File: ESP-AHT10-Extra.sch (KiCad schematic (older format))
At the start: 19 parts, among them J1 USB, SW1 RESET, SW2 PROG, U1 CH330N, U2 HT7233, U3 ESP-12, U4 AHT10

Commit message: 3mm shorter
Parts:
- SW1, SW2: footprint CPB:SW_PUSH_4.5mm -> CPB:Tact Switch 6mmx3.5mm C318817
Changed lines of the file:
@@
 F 0 "SW2" V 4104 6548 50  0000 L CNN
 F 1 "PROG" V 4195 6548 50  0000 L CNN
-F 2 "CPB:SW_PUSH_4.5mm" H 4150 6600 50  0001 C CNN
+F 2 "CPB:Tact Switch 6mmx3.5mm C318817" H 4150 6600 50  0001 C CNN
 F 3 "" H 4150 6600 50  0001 C CNN
 	1    4150 6400
@@
 F 0 "SW1" V 1504 6548 50  0000 L CNN
 F 1 "RESET" V 1595 6548 50  0000 L CNN
-F 2 "CPB:SW_PUSH_4.5mm" H 1550 6600 50  0001 C CNN
+F 2 "CPB:Tact Switch 6mmx3.5mm C318817" H 1550 6600 50  0001 C CNN
 F 3 "" H 1550 6600 50  0001 C CNN
 	1    1550 6400

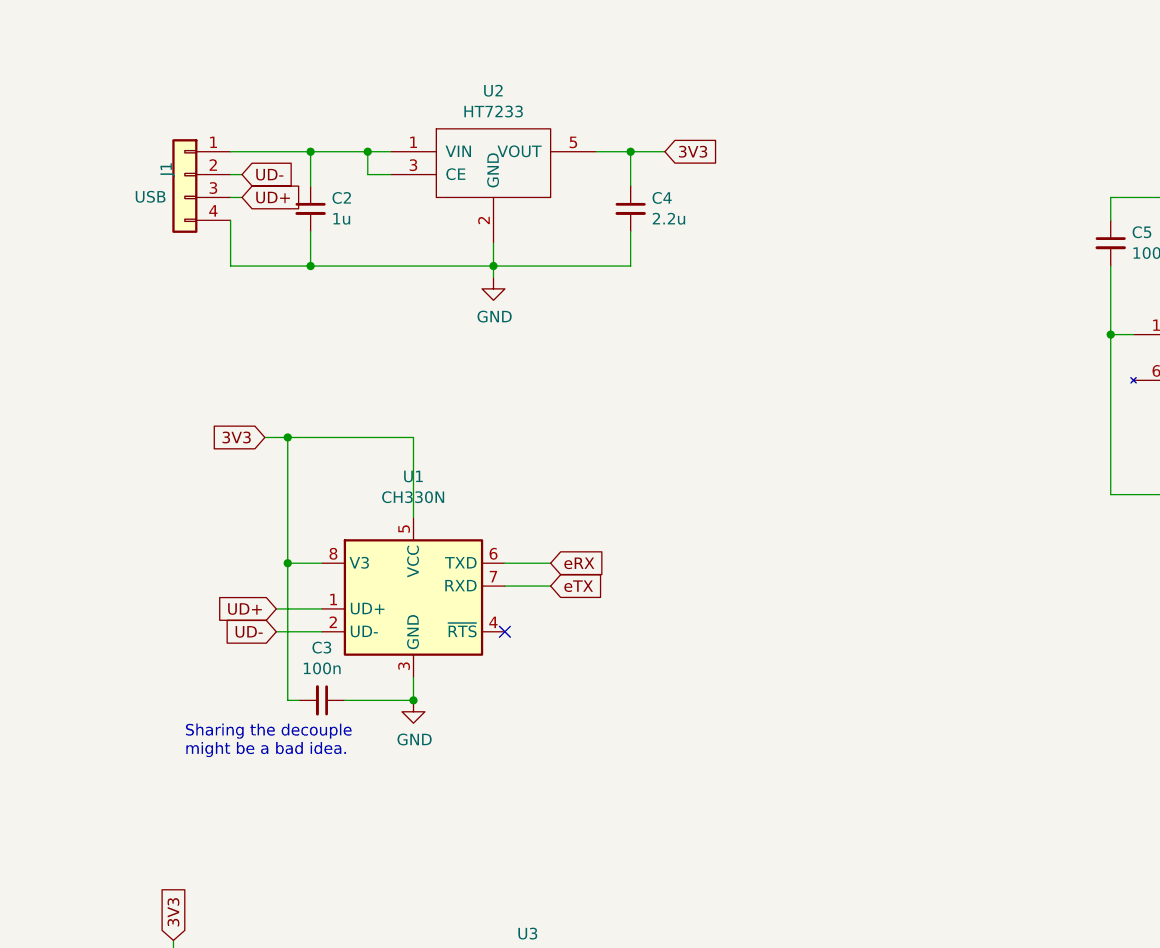
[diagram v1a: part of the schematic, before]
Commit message: add USB ESD protection
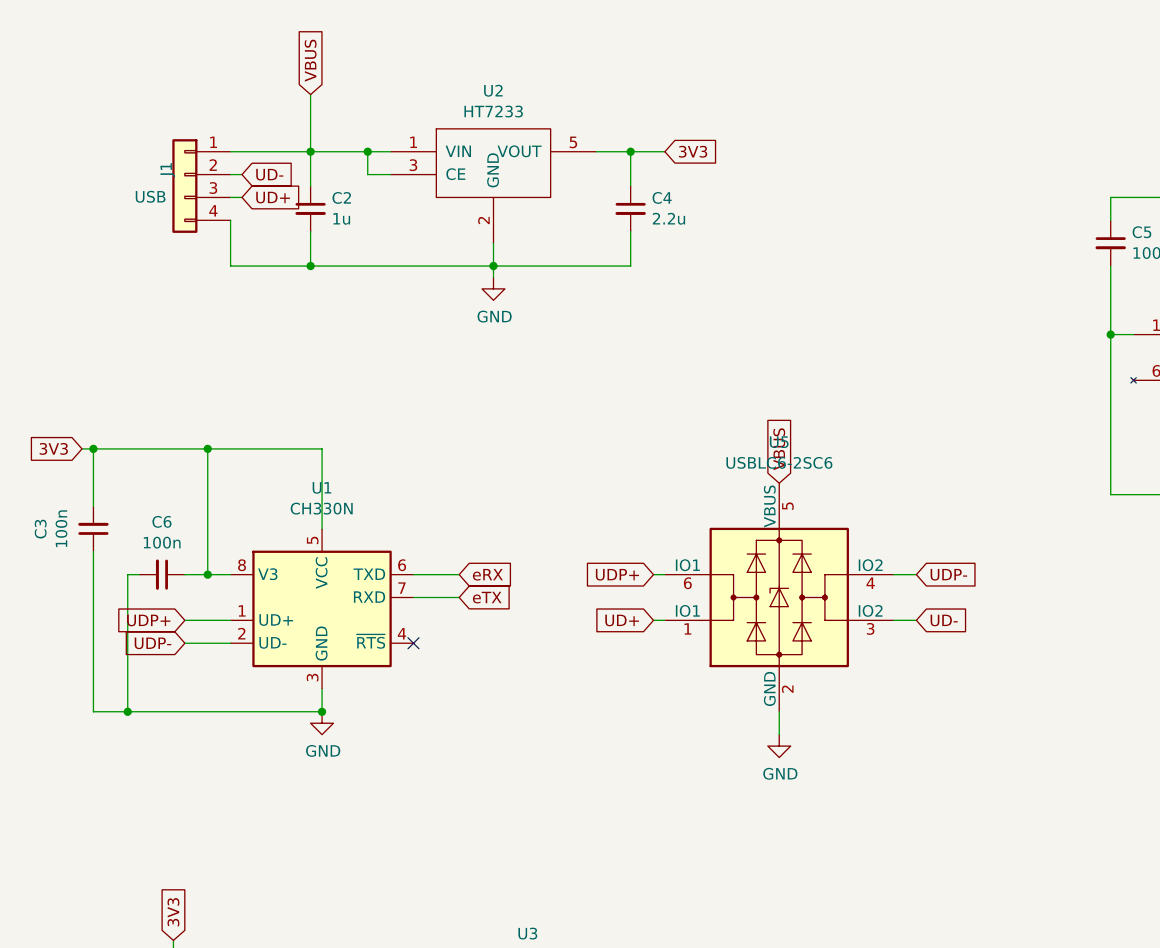
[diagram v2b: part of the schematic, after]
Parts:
- added C6: 100n, Capacitors_SMD:C_0805, symbol Device:C_Small
- added U5: USBLC6-2SC6, Package_TO_SOT_SMD:SOT-23-6, symbol Power_Protection:USBLC6-2SC6
- U4: footprint CPB:AHT10 -> CPB:AHT10-HandSolder
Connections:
- net 3V3: now also C6.1
- net GND: now also C6.2, U5.2 (GND)
- net UD+: now also U5.1 (IO1); no longer U1.1 (UD+)
- net UD-: now also U5.3 (IO2); no longer U1.2 (UD-)
- net VBUS: now reaches C2.1, J1.1 (Pin_1), U2.1 (VIN), U2.3 (CE)
- net VBUS: now also U5.5 (VBUS)
- new net UDP+: U1.1 (UD+), U5.6 (IO1)
- new net UDP-: U1.2 (UD-), U5.4 (IO2)
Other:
- note removed: "Sharing the decouple\nmight be a bad idea."
- moved on the sheet: C3, U1
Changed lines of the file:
@@
 F 0 "U4" H 5650 1750 50  0000 C CNN
 F 1 "AHT10" H 6300 1750 50  0000 C CNN
-F 2 "CPB:AHT10" H 6000 2200 50  0001 C CNN
+F 2 "CPB:AHT10-HandSolder" H 6000 2200 50  0001 C CNN
 F 3 "" H 6000 2200 50  0001 C CNN
 	1    6000 2200
@@
 L Interface_USB:CH330N U1
 U 1 1 5DC02823
-P 2250 3200
-F 0 "U1" H 2250 3678 50  0000 C CNN
-F 1 "CH330N" H 2250 3587 50  0000 C CNN
-F 2 "Package_SO:SOIC-8_3.9x4.9mm_P1.27mm" H 2100 3950 50  0001 C CNN
-F 3 "http://www.wch.cn/downloads/file/240.html" H 2150 3400 50  0001 C CNN
-	1    2250 3200
+P 1850 3250
+F 0 "U1" H 1850 3728 50  0000 C CNN
+F 1 "CH330N" H 1850 3637 50  0000 C CNN
+F 2 "Package_SO:SOIC-8_3.9x4.9mm_P1.27mm" H 1700 4000 50  0001 C CNN
+F 3 "http://www.wch.cn/downloads/file/240.html" H 1750 3450 50  0001 C CNN
+	1    1850 3250
 	1    0    0    -1
 $EndComp
@@
 Wire Wire Line
 	1450 1500 1500 1500
-Text GLabel 1650 3400 0    50   Input ~ 0
+Text GLabel 4450 3350 2    50   Input ~ 0
 UD-
-Text GLabel 1650 3300 0    50   Input ~ 0
+Text GLabel 3300 3350 0    50   Input ~ 0
 UD+
 Wire Wire Line
-	1650 3300 1850 3300
-Wire Wire Line
-	1650 3400 1850 3400
-NoConn ~ 2650 3400
+	1250 3350 1450 3350
+Wire Wire Line
+	1250 3450 1450 3450
+NoConn ~ 2250 3450
 $Comp
 L power:GND #PWR01
 U 1 1 5DC098ED
-P 2250 3700
-F 0 "#PWR01" H 2250 3450 50  0001 C CNN
-F 1 "GND" H 2255 3527 50  0000 C CNN
-F 2 "" H 2250 3700 50  0001 C CNN
-F 3 "" H 2250 3700 50  0001 C CNN
-	1    2250 3700
-	1    0    0    -1
-$EndComp
-Text GLabel 1600 2550 0    50   Input ~ 0
+P 1850 3750
+F 0 "#PWR01" H 1850 3500 50  0001 C CNN
+F 1 "GND" H 1855 3577 50  0000 C CNN
+F 2 "" H 1850 3750 50  0001 C CNN
+F 3 "" H 1850 3750 50  0001 C CNN
+	1    1850 3750
+	1    0    0    -1
+$EndComp
+Text GLabel 800  2600 0    50   Input ~ 0
 3V3
 Wire Wire Line
-	1600 2550 1700 2550
-Wire Wire Line
-	2250 2550 2250 2900
-Wire Wire Line
-	1700 2550 1700 3100
-Wire Wire Line
-	1700 3100 1850 3100
-Connection ~ 1700 2550
-Wire Wire Line
-	1700 2550 2250 2550
+	1850 2600 1850 2950
 $Comp
 L Device:C_Small C3
 U 1 1 5DC0C395
-P 1850 3700
-F 0 "C3" V 1621 3700 50  0000 C CNN
-F 1 "100n" V 1712 3700 50  0000 C CNN
-F 2 "Capacitors_SMD:C_0805" H 1850 3700 50  0001 C CNN
-F 3 "~" H 1850 3700 50  0001 C CNN
-	1    1850 3700
-	0    1    1    0
-$EndComp
-Wire Wire Line
-	1700 3100 1700 3700
-Wire Wire Line
-	1700 3700 1750 3700
-Connection ~ 1700 3100
-Wire Wire Line
-	1950 3700 2250 3700
-Wire Wire Line
-	2250 3600 2250 3700
-Connection ~ 2250 3700
-Text GLabel 2850 3200 2    50   Input ~ 0
+P 850 2950
+F 0 "C3" V 621 2950 50  0000 C CNN
+F 1 "100n" V 712 2950 50  0000 C CNN
+F 2 "Capacitors_SMD:C_0805" H 850 2950 50  0001 C CNN
+F 3 "~" H 850 2950 50  0001 C CNN
+	1    850  2950
+	1    0    0    1
+$EndComp
+Wire Wire Line
+	1850 3650 1850 3750
+Connection ~ 1850 3750
+Text GLabel 2450 3250 2    50   Input ~ 0
 eTX
-Text GLabel 2850 3100 2    50   Input ~ 0
+Text GLabel 2450 3150 2    50   Input ~ 0
 eRX
 Wire Wire Line
-	2650 3100 2850 3100
-Wire Wire Line
-	2650 3200 2850 3200
+	2250 3150 2450 3150
+Wire Wire Line
+	2250 3250 2450 3250
 $Comp
 L Switch:SW_Push SW2
@@
 Wire Wire Line
 	1550 6700 2750 6700
-Text Notes 1250 3950 0    50   ~ 0
-Sharing the decouple\nmight be a bad idea.
+$Comp
+L Device:C_Small C6
+U 1 1 5DC2141A
+P 1150 3150
+F 0 "C6" V 921 3150 50  0000 C CNN
+F 1 "100n" V 1012 3150 50  0000 C CNN
+F 2 "Capacitors_SMD:C_0805" H 1150 3150 50  0001 C CNN
+F 3 "~" H 1150 3150 50  0001 C CNN
+	1    1150 3150
+	0    1    1    0
+$EndComp
+Wire Wire Line
+	800  2600 850  2600
+Wire Wire Line
+	850  2850 850  2600
+Connection ~ 850  2600
+Wire Wire Line
+	850  3050 850  3750
+Wire Wire Line
+	850  3750 1000 3750
+Wire Wire Line
+	1050 3150 1000 3150
+Wire Wire Line
+	1000 3150 1000 3750
+Wire Wire Line
+	1000 3750 1850 3750
+$Comp
+L Power_Protection:USBLC6-2SC6 U5
+U 1 1 5DC39FB1
+P 3850 3250
+F 0 "U5" H 3850 3928 50  0000 C CNN
+F 1 "USBLC6-2SC6" H 3850 3837 50  0000 C CNN
+F 2 "Package_TO_SOT_SMD:SOT-23-6" H 3100 3650 50  0001 C CNN
+F 3 "http://www2.st.com/resource/en/datasheet/CD00050750.pdf" H 4050 3600 50  0001 C CNN
+	1    3850 3250
+	1    0    0    -1
+$EndComp
+Text GLabel 1250 3350 0    50   Input ~ 0
+UDP+
+Text GLabel 1250 3450 0    50   Input ~ 0
+UDP-
+Connection ~ 1000 3750
+Wire Wire Line
+	1250 3150 1350 3150
+$Comp
+L power:GND #PWR05
+U 1 1 5DC4A8A6
+P 3850 3850
+F 0 "#PWR05" H 3850 3600 50  0001 C CNN
+F 1 "GND" H 3855 3677 50  0000 C CNN
+F 2 "" H 3850 3850 50  0001 C CNN
+F 3 "" H 3850 3850 50  0001 C CNN
+	1    3850 3850
+	1    0    0    -1
+$EndComp
+Wire Wire Line
+	1800 1050 1800 1300
+Text GLabel 1800 1050 1    50   Input ~ 0
+VBUS
+Text GLabel 3850 2750 1    50   Input ~ 0
+VBUS
+Text GLabel 3300 3150 0    50   Input ~ 0
+UDP+
+Text GLabel 4450 3150 2    50   Input ~ 0
+UDP-
+Wire Wire Line
+	3300 3150 3350 3150
+Wire Wire Line
+	3300 3350 3350 3350
+Wire Wire Line
+	4350 3150 4450 3150
+Wire Wire Line
+	4350 3350 4450 3350
+Wire Wire Line
+	3850 3750 3850 3850
+Wire Wire Line
+	850  2600 1350 2600
+Wire Wire Line
+	1350 2600 1350 3150
+Connection ~ 1350 2600
+Wire Wire Line
+	1350 2600 1850 2600
+Connection ~ 1350 3150
+Wire Wire Line
+	1350 3150 1450 3150
 $EndSCHEMATC

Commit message: add a fuse. Don't need to fry another sensor...
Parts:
- added F1: 500mA, Fuse:Fuse_0805_2012Metric, symbol Device:Fuse_Small
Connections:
- wire segments 97 -> 100
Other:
- moved on the sheet: J1
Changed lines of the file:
@@
 L Connector_Generic:Conn_01x04 J1
 U 1 1 5DBDB3F6
-P 1250 1400
-F 0 "J1" V 1330 1392 50  0000 L CNN
-F 1 "USB" H 1330 1301 50  0000 L CNN
-F 2 "CPB:usb-PCB" H 1250 1400 50  0001 C CNN
-F 3 "~" H 1250 1400 50  0001 C CNN
-	1    1250 1400
+P 900 1400
+F 0 "J1" V 980 1392 50  0000 L CNN
+F 1 "USB" H 980 1301 50  0000 L CNN
+F 2 "CPB:usb-PCB" H 900 1400 50  0001 C CNN
+F 3 "~" H 900 1400 50  0001 C CNN
+	1    900  1400
 	-1   0    0    -1
 $EndComp
@@
 Wire Wire Line
 	1800 1300 1800 1450
-Connection ~ 1800 1300
 Wire Wire Line
 	1800 1300 2050 1300
@@
 	1450 1800 1800 1800
 Connection ~ 1800 1800
-Wire Wire Line
-	1450 1300 1800 1300
 Text GLabel 7000 2300 2    50   Input ~ 0
 SCL
@@
 Text GLabel 1500 1500 2    50   Input ~ 0
 UD+
-Wire Wire Line
-	1450 1400 1500 1400
-Wire Wire Line
-	1450 1500 1500 1500
 Text GLabel 4450 3350 2    50   Input ~ 0
 UD-
@@
 	1    0    0    -1
 $EndComp
-Wire Wire Line
-	1800 1050 1800 1300
-Text GLabel 1800 1050 1    50   Input ~ 0
+Text GLabel 2100 1050 2    50   Output ~ 0
 VBUS
 Text GLabel 3850 2750 1    50   Input ~ 0
@@
 Wire Wire Line
 	1350 3150 1450 3150
+$Comp
+L Device:Fuse_Small F1
+U 1 1 5DC64535
+P 1400 1300
+F 0 "F1" H 1400 1485 50  0000 C CNN
+F 1 "500mA" H 1400 1394 50  0000 C CNN
+F 2 "Fuse:Fuse_0805_2012Metric" H 1400 1300 50  0001 C CNN
+F 3 "~" H 1400 1300 50  0001 C CNN
+	1    1400 1300
+	1    0    0    -1
+$EndComp
+Wire Wire Line
+	1100 1300 1300 1300
+Wire Wire Line
+	1100 1400 1500 1400
+Wire Wire Line
+	1100 1500 1500 1500
+Wire Wire Line
+	1100 1600 1450 1600
+Wire Wire Line
+	1500 1300 1800 1300
+Connection ~ 1800 1300
+Wire Wire Line
+	2050 1050 2050 1300
+Wire Wire Line
+	2050 1050 2100 1050
 $EndSCHEMATC

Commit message: more tweaking
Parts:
- removed F1: 500mA, Fuse:Fuse_0805_2012Metric, symbol Device:Fuse_Small
- added C7: 100n, Capacitors_SMD:C_0805, symbol Device:C_Small
- added F1: 200mA, Fuse:Fuse_0805_2012Metric, symbol Device:Polyfuse_Small
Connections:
- net labels added: 5V
- wire segments 100 -> 101
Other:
- note added: "NOTE: maybe overkill; I can't\nfind an example of a board\nwith WCH chips and ESD\nprotection.\nTermination resistors (22R?)\nmight also not be a bad idea."
- moved on the sheet: C2, C3, C4, C5, C6, J1, R6, R7, U1, U2, U4, U5

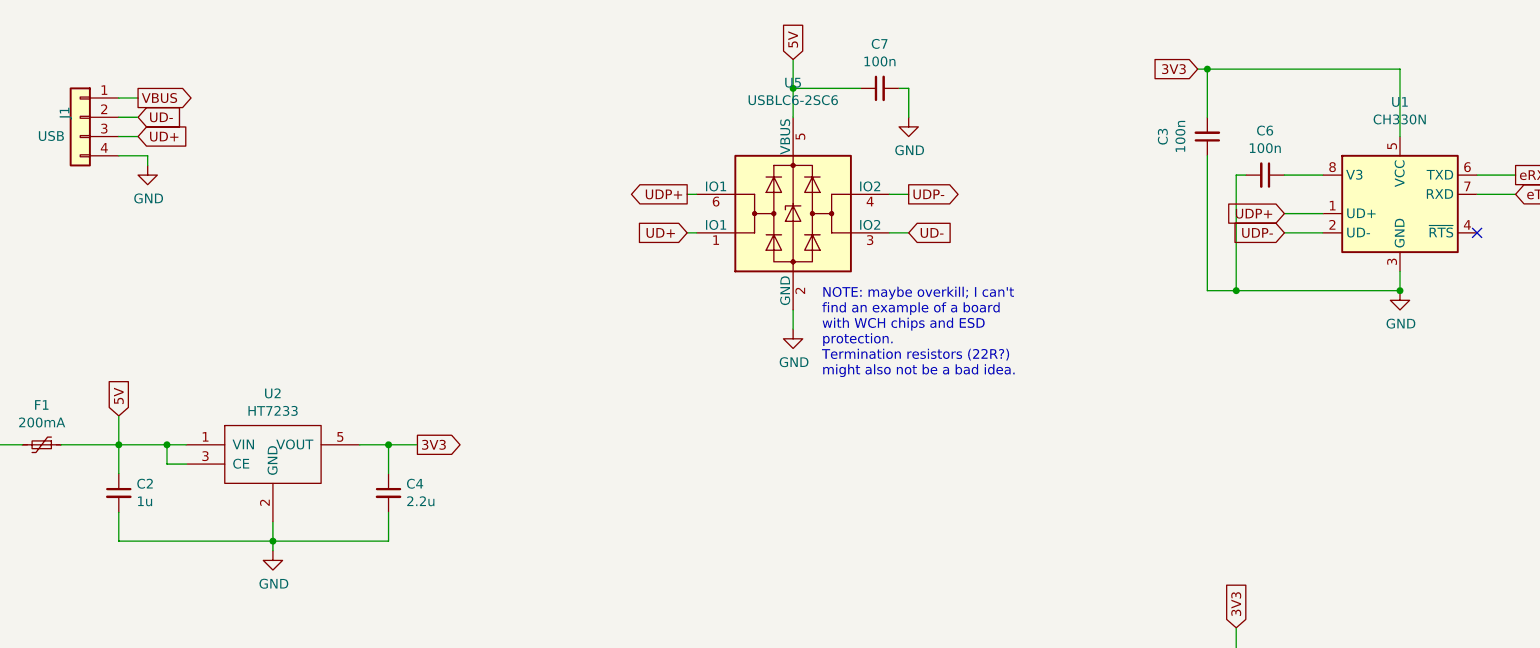
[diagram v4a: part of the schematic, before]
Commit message: fix V3 connections to CH330N, bump the bulk caps to 10uF, rev number
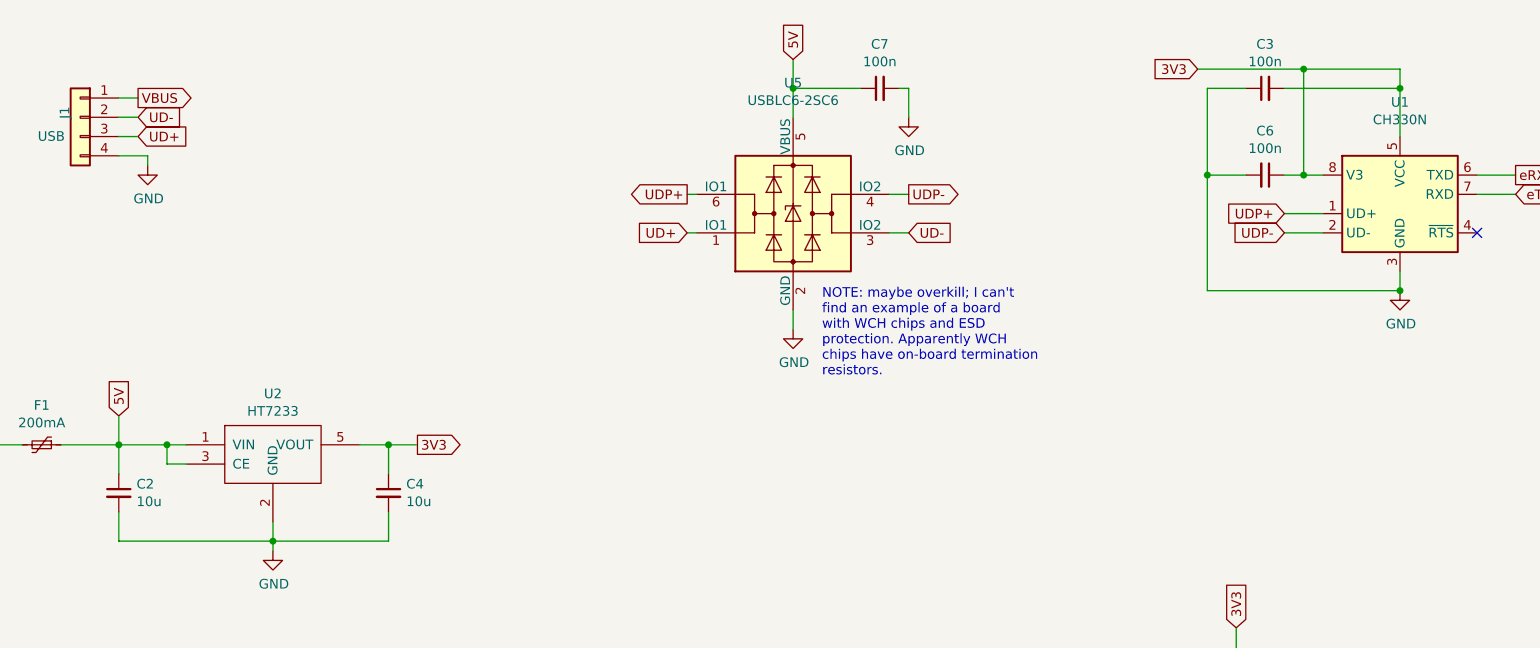
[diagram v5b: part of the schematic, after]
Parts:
- C2: value 1u -> 10u
- C4: value 2.2u -> 10u
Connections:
- net 3V3: now also C6.1, U1.8 (V3)
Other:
- note added: "NOTE: maybe overkill; I can't\nfind an example of a board\nwith WCH chips and ESD\nprotection. Apparently WCH\nchips have on-board termination\nresistors."
- note removed: "NOTE: maybe overkill; I can't\nfind an example of a board\nwith WCH chips and ESD\nprotection.\nTermination resistors (22R?)\nmight also not be a bad idea."
- moved on the sheet: C3
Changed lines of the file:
@@
 P 1950 3300
 F 0 "C2" H 2042 3346 50  0000 L CNN
-F 1 "1u" H 2042 3255 50  0000 L CNN
+F 1 "10u" H 2042 3255 50  0000 L CNN
 F 2 "Capacitors_SMD:C_0805" H 1950 3300 50  0001 C CNN
 F 3 "~" H 1950 3300 50  0001 C CNN
@@
 P 3350 3300
 F 0 "C4" H 3442 3346 50  0000 L CNN
-F 1 "2.2u" H 3442 3255 50  0000 L CNN
+F 1 "10u" H 3442 3255 50  0000 L CNN
 F 2 "Capacitors_SMD:C_0805" H 3350 3300 50  0001 C CNN
 F 3 "~" H 3350 3300 50  0001 C CNN
@@
 3V3
 Wire Wire Line
-	8600 1100 8600 1450
+	8600 1100 8600 1200
 $Comp
 L Device:C_Small C3
 U 1 1 5DC0C395
-P 7600 1450
-F 0 "C3" V 7371 1450 50  0000 C CNN
-F 1 "100n" V 7462 1450 50  0000 C CNN
-F 2 "Capacitors_SMD:C_0805" H 7600 1450 50  0001 C CNN
-F 3 "~" H 7600 1450 50  0001 C CNN
-	1    7600 1450
-	1    0    0    1
+P 7900 1200
+F 0 "C3" V 7671 1200 50  0000 C CNN
+F 1 "100n" V 7762 1200 50  0000 C CNN
+F 2 "Capacitors_SMD:C_0805" H 7900 1200 50  0001 C CNN
+F 3 "~" H 7900 1200 50  0001 C CNN
+	1    7900 1200
+	0    -1   1    0
 $EndComp
 Wire Wire Line
@@
 	0    1    1    0
 $EndComp
-Wire Wire Line
-	7550 1100 7600 1100
-Wire Wire Line
-	7600 1350 7600 1100
-Connection ~ 7600 1100
-Wire Wire Line
-	7600 1550 7600 2250
-Wire Wire Line
-	7600 2250 7750 2250
-Wire Wire Line
-	7800 1650 7750 1650
-Wire Wire Line
-	7750 1650 7750 2250
-Wire Wire Line
-	7750 2250 8600 2250
 $Comp
 L Power_Protection:USBLC6-2SC6 U5
@@
 Text GLabel 8000 1950 0    50   Input ~ 0
 UDP-
-Connection ~ 7750 2250
 $Comp
 L power:GND #PWR05
@@
 $EndComp
 Wire Wire Line
-	7600 1100 8600 1100
-Wire Wire Line
-	8000 1650 8200 1650
+	8000 1650 8100 1650
 $Comp
 L power:GND #PWR0101
@@
 	6050 1200 6050 1350
 Text Notes 5600 2700 0    50   ~ 0
-NOTE: maybe overkill; I can't\nfind an example of a board\nwith WCH chips and ESD\nprotection.\nTermination resistors (22R?)\nmight also not be a bad idea.
+NOTE: maybe overkill; I can't\nfind an example of a board\nwith WCH chips and ESD\nprotection. Apparently WCH\nchips have on-board termination\nresistors.
+Wire Wire Line
+	8100 1650 8100 1100
+Connection ~ 8100 1650
+Wire Wire Line
+	8100 1650 8200 1650
+Connection ~ 8100 1100
+Wire Wire Line
+	8100 1100 8600 1100
+Wire Wire Line
+	7550 1100 8100 1100
+Wire Wire Line
+	7600 1200 7800 1200
+Wire Wire Line
+	7600 1200 7600 1650
+Wire Wire Line
+	8000 1200 8600 1200
+Connection ~ 8600 1200
+Wire Wire Line
+	8600 1200 8600 1450
+Wire Wire Line
+	7600 2250 8600 2250
+Wire Wire Line
+	7800 1650 7600 1650
+Connection ~ 7600 1650
+Wire Wire Line
+	7600 1650 7600 2250
 $EndSCHEMATC
